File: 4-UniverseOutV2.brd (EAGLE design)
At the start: 102 x 69 mm, 45 parts, among them IC1 MAX481, IC2 MAX481, IC3 MAX481, IC4 MAX481, U1 MC3FAH1, U2 MC3FAH1, U3 MC3FAH1, U4 MC3FAH1

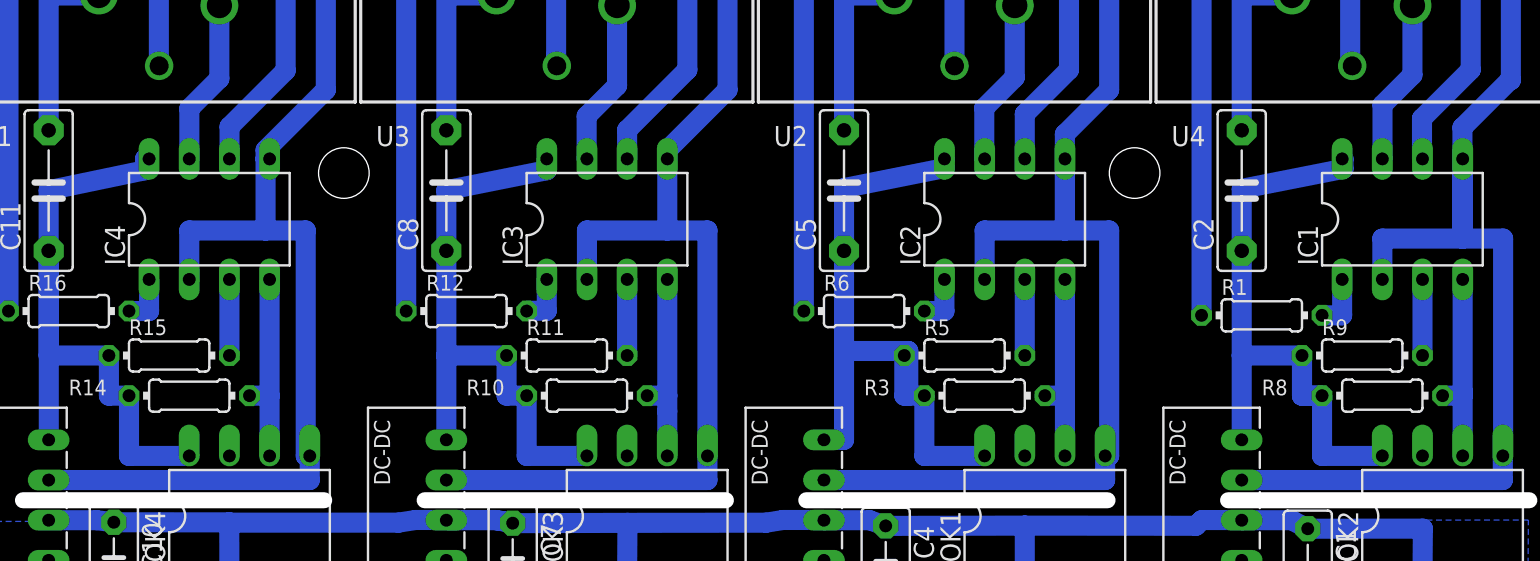
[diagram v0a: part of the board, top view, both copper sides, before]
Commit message: Add files via upload
Added 120ohm resistors
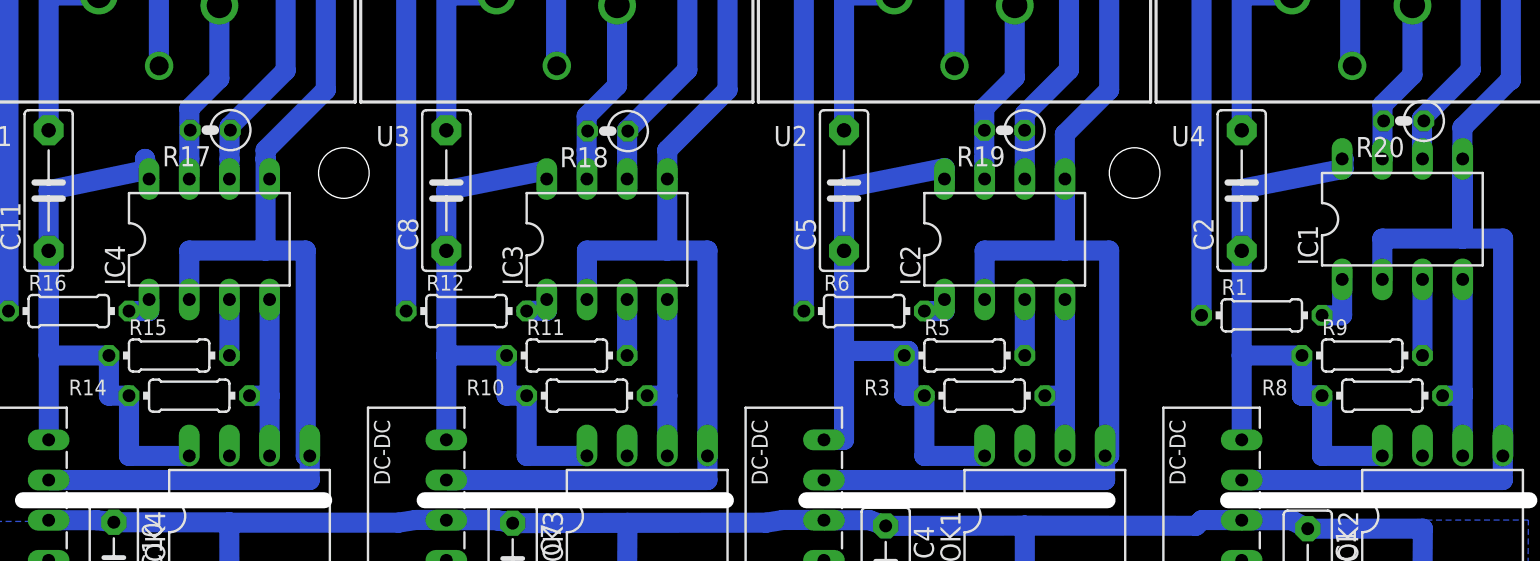
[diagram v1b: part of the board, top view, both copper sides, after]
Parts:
- added R17, R18, R19, R20: 120, resistor:0207/2V
- moved IC2 1.27 mm to (65.8, 38.8)
- moved IC3 1.27 mm to (40.6, 38.8)
- moved IC4 1.27 mm to (15.5, 38.8)
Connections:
- net N$161: now also R20.1
- net N$162: now also R20.2
- net N$169: now also R19.1
- net N$170: now also R19.2
- net N$179: now also R18.1
- net N$181: now also R18.2
- net N$193: now also R17.1
- net N$194: now also R17.2
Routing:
- net N$169: track 35.3 -> 40.8 mm
- net N$194: track 10.5 -> 14.8 mm
- net N$179: track 36.8 -> 40.5 mm
- net N$181: track 10.5 -> 14.2 mm
- net N$193: track 36.7 -> 40.3 mm
- net N$170: track 10.5 -> 14.1 mm
- net N$161: track 35.7 -> 38.2 mm
- net N$162: track 10.5 -> 12.4 mm
- net N$196: track 3.27 -> 2.00 mm
- net N$192: track 12.4 -> 11.2 mm
- net N$191: track 4.81 -> 3.54 mm
- net N$187: track 3.27 -> 2.00 mm
- net N$178: track 12.4 -> 11.2 mm
- net N$177: track 4.81 -> 3.54 mm
- net N$172: track 3.27 -> 2.00 mm
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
